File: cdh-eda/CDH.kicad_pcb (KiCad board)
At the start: 2 copper layers, 96 x 90 mm, 23 parts, among them J1 THD-20-R, J4 USB_OTG, P1 S04B-PASK-2(LF)(SN), P2 S04B-PASK-2(LF)(SN), U1 ATA6560-GAQW-VAO, U2 TPD2EUSB30, U3 MCP2510-E/SO, U4 74LVC1G07SE-7

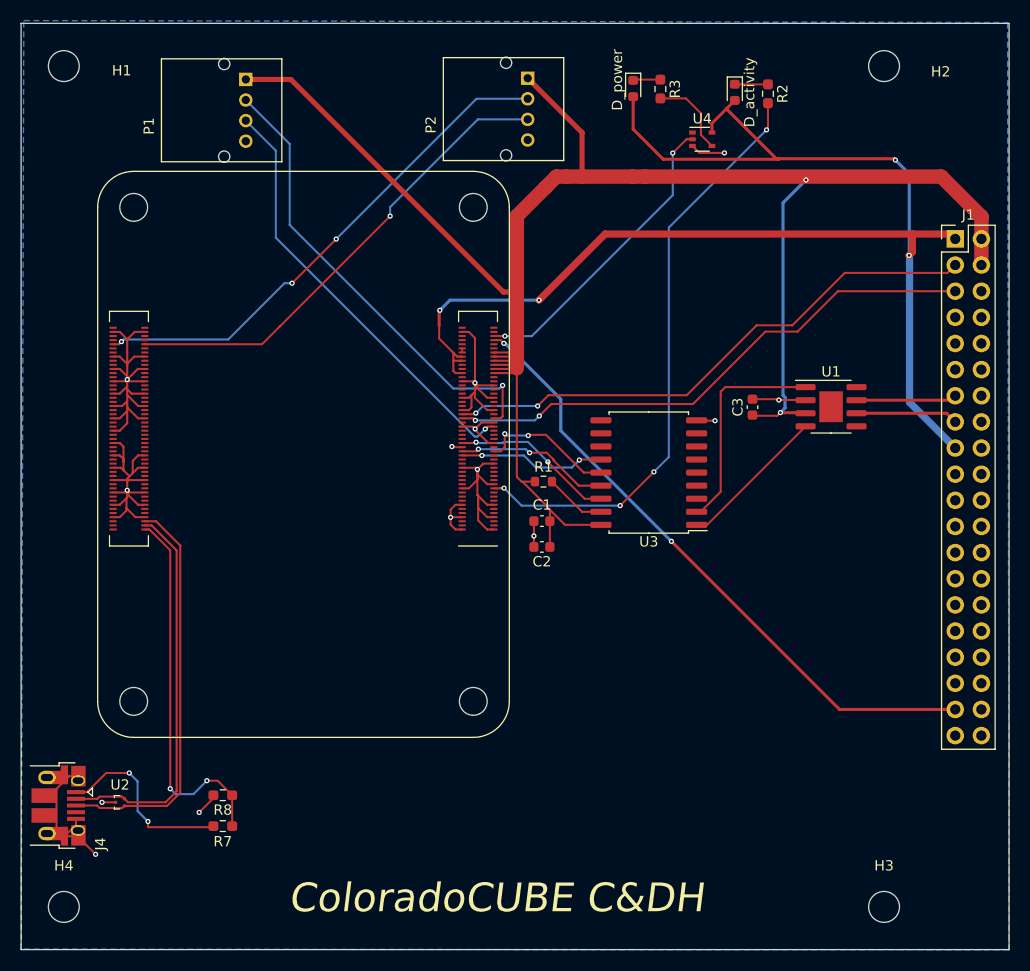
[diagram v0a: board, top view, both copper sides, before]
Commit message: V.2 updates
 1. Add jumper CAN resistors
 2. Add camera connector
 3. Add display connector
 5. Updated CAN transceiver protective circuitry
 6. Add MCP2515 interrupt GPIO pin 18
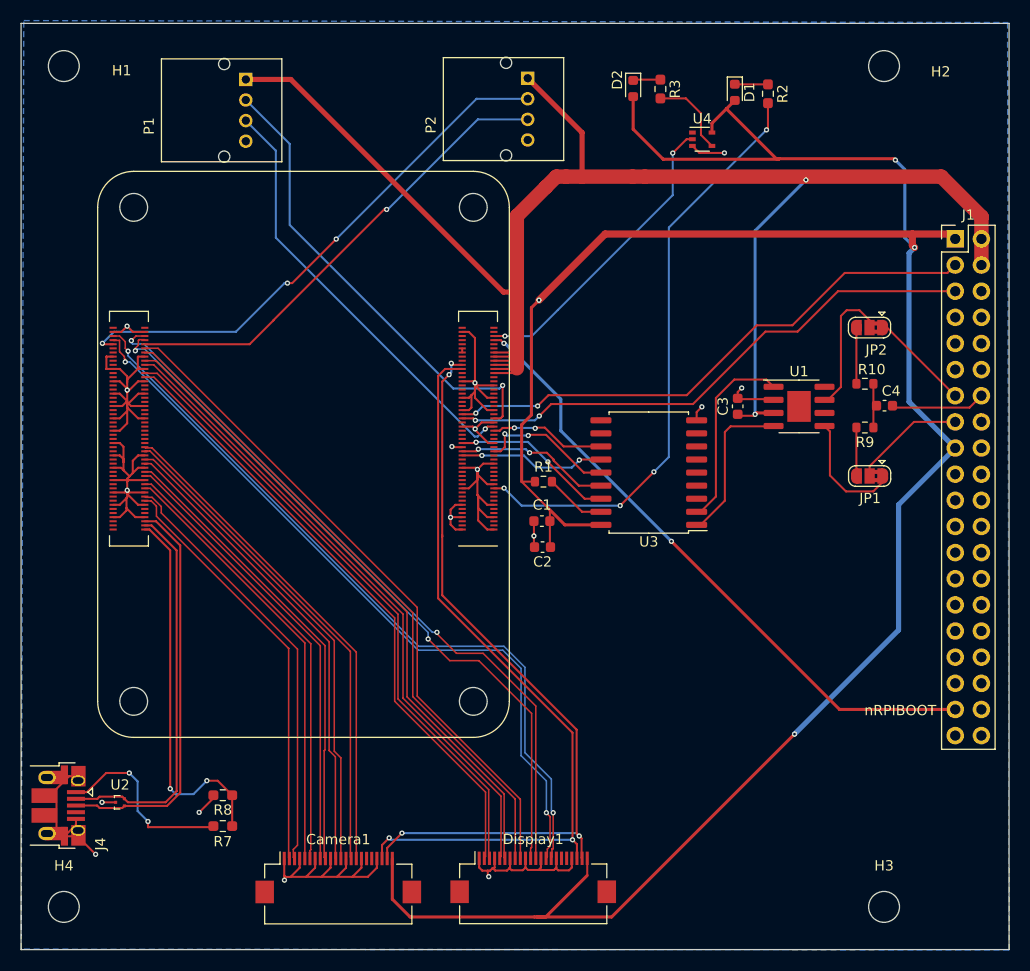
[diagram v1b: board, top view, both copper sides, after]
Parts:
- added C4: 4.7nF, Capacitor_SMD:C_0603_1608Metric, F.Cu at (190.4, 93.2)
- added Camera1: Conn_01x22_Female, Connector_FFC-FPC:Hirose_FH12-22S-0.5SH_1x22-1MP_P0.50mm_Horizontal, F.Cu at (137.3, 139.0)
- added Display1: Conn_01x22_Female, Connector_FFC-FPC:Hirose_FH12-22S-0.5SH_1x22-1MP_P0.50mm_Horizontal, F.Cu at (156.2, 139.0)
- added JP1: SolderJumper_3_Bridged12, Jumper:SolderJumper-3_P1.3mm_Bridged2Bar12_RoundedPad1.0x1.5mm, F.Cu at (188.9, 100.0)
- added JP2: SolderJumper_3_Bridged12, Jumper:SolderJumper-3_P1.3mm_Bridged2Bar12_RoundedPad1.0x1.5mm, F.Cu at (188.9, 85.6)
- added R10: 60, Resistor_SMD:R_0603_1608Metric, F.Cu at (188.5, 91.0)
- added R9: 60, Resistor_SMD:R_0603_1608Metric, F.Cu at (188.5, 95.3)
- Module1: value DF40GB-10DP-0.4V(51) -> ComputeModule4-CM4
- U2: value TPD2EUSB30 -> TPD2EUSB30ADRTR
- U3: value MCP2510-E/SO -> MCP2515T-I/SO
- moved U1 3.11 mm to (182.1, 93.2)
- moved C3 1.44 mm to (176.1, 93.2)
- moved C2 0.06 mm to (157.2, 106.9)
- renumbered D_activity to D1, D_power to D2
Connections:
- C1 pad 1: +5V -> +3.3V
- C2 pad 1: +5V -> +3.3V
- J1 pad 10: (no net) -> unconnected-(J1-Pad10)
- J1 pad 25: GND -> unconnected-(J1-Pad25)
- J1 pad 8: (no net) -> unconnected-(J1-Pad8)
- J1 pad 9: GND -> unconnected-(J1-Pad9)
- Module1 pad 10: Net-(Module1-Pad10) -> (no net)
- Module1 pad 100: Net-(Module1-Pad100) -> (no net)
- Module1 pad 102: Net-(Module1-Pad102) -> unconnected-(Module1-Pad102)
- Module1 pad 104: Net-(Module1-Pad104) -> unconnected-(Module1-Pad104)
- Module1 pad 106: Net-(Module1-Pad106) -> unconnected-(Module1-Pad106)
- Module1 pad 109: Net-(Module1-Pad109) -> unconnected-(Module1-Pad109)
- Module1 pad 11: Net-(Module1-Pad11) -> (no net)
- Module1 pad 110: Net-(Module1-Pad110) -> unconnected-(Module1-Pad110)
- Module1 pad 111: Net-(Module1-Pad111) -> unconnected-(Module1-Pad111)
- Module1 pad 112: Net-(Module1-Pad112) -> unconnected-(Module1-Pad112)
- Module1 pad 115: Net-(Module1-Pad115) -> /CM4 High Speed/CAM1_D0_N
- Module1 pad 116: Net-(Module1-Pad116) -> unconnected-(Module1-Pad116)
- Module1 pad 117: Net-(Module1-Pad117) -> /CM4 High Speed/CAM1_D0_P
- Module1 pad 118: Net-(Module1-Pad118) -> unconnected-(Module1-Pad118)
- Module1 pad 12: Net-(Module1-Pad12) -> (no net)
- Module1 pad 121: Net-(Module1-Pad121) -> /CM4 High Speed/CAM1_D1_N
- Module1 pad 122: Net-(Module1-Pad122) -> unconnected-(Module1-Pad122)
- Module1 pad 123: Net-(Module1-Pad123) -> /CM4 High Speed/CAM1_D1_P
- Module1 pad 124: Net-(Module1-Pad124) -> unconnected-(Module1-Pad124)
- Module1 pad 127: Net-(Module1-Pad127) -> /CM4 High Speed/CAM1_C_N
- Module1 pad 128: Net-(Module1-Pad128) -> unconnected-(Module1-Pad128)
- Module1 pad 129: Net-(Module1-Pad129) -> /CM4 High Speed/CAM1_C_P
- Module1 pad 130: Net-(Module1-Pad130) -> unconnected-(Module1-Pad130)
- Module1 pad 133: Net-(Module1-Pad133) -> /CM4 High Speed/CAM1_D2_N
- Module1 pad 134: Net-(Module1-Pad134) -> unconnected-(Module1-Pad134)
- Module1 pad 135: Net-(Module1-Pad135) -> /CM4 High Speed/CAM1_D2_P
- Module1 pad 136: Net-(Module1-Pad136) -> unconnected-(Module1-Pad136)
- Module1 pad 139: Net-(Module1-Pad139) -> /CM4 High Speed/CAM1_D3_N
- Module1 pad 140: Net-(Module1-Pad140) -> unconnected-(Module1-Pad140)
- Module1 pad 141: Net-(Module1-Pad141) -> /CM4 High Speed/CAM1_D3_P
- Module1 pad 142: Net-(Module1-Pad142) -> unconnected-(Module1-Pad142)
- Module1 pad 143: Net-(Module1-Pad143) -> unconnected-(Module1-Pad143)
- Module1 pad 145: Net-(Module1-Pad145) -> unconnected-(Module1-Pad145)
- Module1 pad 146: Net-(Module1-Pad146) -> unconnected-(Module1-Pad146)
- Module1 pad 147: Net-(Module1-Pad147) -> unconnected-(Module1-Pad147)
- Module1 pad 148: Net-(Module1-Pad148) -> unconnected-(Module1-Pad148)
- Module1 pad 149: Net-(Module1-Pad149) -> unconnected-(Module1-Pad149)
- Module1 pad 15: Net-(Module1-Pad15) -> (no net)
- Module1 pad 151: Net-(Module1-Pad151) -> unconnected-(Module1-Pad151)
- Module1 pad 152: Net-(Module1-Pad152) -> unconnected-(Module1-Pad152)
- Module1 pad 153: Net-(Module1-Pad153) -> unconnected-(Module1-Pad153)
- Module1 pad 154: Net-(Module1-Pad154) -> unconnected-(Module1-Pad154)
- Module1 pad 157: Net-(Module1-Pad157) -> unconnected-(Module1-Pad157)
- Module1 pad 158: Net-(Module1-Pad158) -> unconnected-(Module1-Pad158)
- Module1 pad 159: Net-(Module1-Pad159) -> unconnected-(Module1-Pad159)
- Module1 pad 16: Net-(Module1-Pad16) -> (no net)
- Module1 pad 160: Net-(Module1-Pad160) -> unconnected-(Module1-Pad160)
- Module1 pad 163: Net-(Module1-Pad163) -> unconnected-(Module1-Pad163)
- Module1 pad 164: Net-(Module1-Pad164) -> unconnected-(Module1-Pad164)
- Module1 pad 165: Net-(Module1-Pad165) -> unconnected-(Module1-Pad165)
- Module1 pad 166: Net-(Module1-Pad166) -> unconnected-(Module1-Pad166)
- Module1 pad 169: Net-(Module1-Pad169) -> unconnected-(Module1-Pad169)
- Module1 pad 17: Net-(Module1-Pad17) -> (no net)
- Module1 pad 170: Net-(Module1-Pad170) -> unconnected-(Module1-Pad170)
- Module1 pad 171: Net-(Module1-Pad171) -> unconnected-(Module1-Pad171)
- Module1 pad 172: Net-(Module1-Pad172) -> unconnected-(Module1-Pad172)
- Module1 pad 175: Net-(Module1-Pad175) -> /CM4 High Speed/DSI1_D0_N
- Module1 pad 176: Net-(Module1-Pad176) -> unconnected-(Module1-Pad176)
- Module1 pad 177: Net-(Module1-Pad177) -> /CM4 High Speed/DSI1_D0_P
- Module1 pad 178: Net-(Module1-Pad178) -> unconnected-(Module1-Pad178)
- Module1 pad 18: Net-(Module1-Pad18) -> (no net)
- Module1 pad 181: Net-(Module1-Pad181) -> /CM4 High Speed/DSI1_D1_N
- Module1 pad 182: Net-(Module1-Pad182) -> unconnected-(Module1-Pad182)
- Module1 pad 183: Net-(Module1-Pad183) -> /CM4 High Speed/DSI1_D1_P
- Module1 pad 184: Net-(Module1-Pad184) -> unconnected-(Module1-Pad184)
- Module1 pad 187: Net-(Module1-Pad187) -> /CM4 High Speed/DSI1_C_N
- Module1 pad 188: Net-(Module1-Pad188) -> unconnected-(Module1-Pad188)
- Module1 pad 189: Net-(Module1-Pad189) -> /CM4 High Speed/DSI1_C_P
- Module1 pad 19: Net-(Module1-Pad19) -> (no net)
- Module1 pad 190: Net-(Module1-Pad190) -> unconnected-(Module1-Pad190)
- Module1 pad 191: /CM4 GPIO/GPIO13 -> GND
- Module1 pad 192: /CM4 GPIO/GPIO12 -> GND
- Module1 pad 193: Net-(Module1-Pad193) -> /CM4 High Speed/DSI1_D2_N
- Module1 pad 194: Net-(Module1-Pad194) -> /CM4 High Speed/DSI1_D3_N
- Module1 pad 195: Net-(Module1-Pad195) -> /CM4 High Speed/DSI1_D2_P
- Module1 pad 196: Net-(Module1-Pad196) -> /CM4 High Speed/DSI1_D3_P
- Module1 pad 199: Net-(Module1-Pad199) -> unconnected-(Module1-Pad199)
- Module1 pad 20: /CM4 GPIO/EEPROM_nWP -> (no net)
- Module1 pad 200: Net-(Module1-Pad200) -> unconnected-(Module1-Pad200)
- Module1 pad 24: Net-(Module1-Pad24) -> (no net)
- Module1 pad 25: Net-(Module1-Pad25) -> (no net)
- Module1 pad 26: Net-(Module1-Pad26) -> (no net)
- Module1 pad 27: Net-(Module1-Pad27) -> (no net)
- Module1 pad 28: Net-(Module1-Pad28) -> (no net)
- Module1 pad 29: Net-(Module1-Pad29) -> (no net)
- Module1 pad 3: Net-(Module1-Pad3) -> (no net)
- Module1 pad 30: Net-(Module1-Pad30) -> (no net)
- Module1 pad 31: Net-(Module1-Pad31) -> (no net)
- Module1 pad 34: Net-(Module1-Pad34) -> (no net)
- Module1 pad 35: Net-(Module1-Pad35) -> (no net)
- Module1 pad 36: Net-(Module1-Pad36) -> (no net)
- Module1 pad 37: /CM4 GPIO/GPIO7 -> (no net)
- Module1 pad 4: Net-(Module1-Pad4) -> (no net)
- Module1 pad 41: Net-(Module1-Pad41) -> (no net)
- Module1 pad 45: Net-(Module1-Pad45) -> (no net)
- Module1 pad 46: Net-(Module1-Pad46) -> (no net)
- Module1 pad 47: Net-(Module1-Pad47) -> (no net)
- Module1 pad 48: Net-(Module1-Pad48) -> (no net)
- Module1 pad 49: Net-(Module1-Pad49) -> /CM4 GPIO/GPIO18
- Module1 pad 5: Net-(Module1-Pad5) -> (no net)
- Module1 pad 50: Net-(Module1-Pad50) -> (no net)
- Module1 pad 54: Net-(Module1-Pad54) -> (no net)
- Module1 pad 57: Net-(Module1-Pad57) -> (no net)
- Module1 pad 6: Net-(Module1-Pad6) -> (no net)
- Module1 pad 61: Net-(Module1-Pad61) -> (no net)
- Module1 pad 62: Net-(Module1-Pad62) -> (no net)
- Module1 pad 63: Net-(Module1-Pad63) -> (no net)
- Module1 pad 64: Net-(Module1-Pad64) -> (no net)
- Module1 pad 67: Net-(Module1-Pad67) -> (no net)
- Module1 pad 68: Net-(Module1-Pad68) -> (no net)
- Module1 pad 69: Net-(Module1-Pad69) -> (no net)
- Module1 pad 70: Net-(Module1-Pad70) -> (no net)
- Module1 pad 72: Net-(Module1-Pad72) -> (no net)
- Module1 pad 73: Net-(Module1-Pad73) -> (no net)
- Module1 pad 75: Net-(Module1-Pad75) -> (no net)
- Module1 pad 76: Net-(Module1-Pad76) -> (no net)
- Module1 pad 78: +3.3V -> (no net)
- Module1 pad 80: Net-(Module1-Pad80) -> /CM4 High Speed/SCL0
- Module1 pad 82: Net-(Module1-Pad82) -> /CM4 High Speed/SDA0
- Module1 pad 84: +3.3V -> (no net)
- Module1 pad 86: +3.3V -> (no net)
- Module1 pad 88: +1.8V -> (no net)
- Module1 pad 89: Net-(Module1-Pad89) -> (no net)
- Module1 pad 9: Net-(Module1-Pad9) -> (no net)
- Module1 pad 90: +1.8V -> (no net)
- Module1 pad 91: Net-(Module1-Pad91) -> (no net)
- Module1 pad 92: Net-(Module1-Pad92) -> (no net)
- Module1 pad 94: Net-(Module1-Pad94) -> (no net)
- Module1 pad 96: Net-(Module1-Pad96) -> (no net)
- Module1 pad 97: Net-(Module1-Pad97) -> (no net)
- Module1 pad 99: Net-(Module1-Pad99) -> (no net)
- R1 pad 1: +5V -> +3.3V
- U1 pad 5: unconnected-(U1-Pad5) -> Net-(U1-Pad5)
- U1 pad 6: Net-(J1-Pad15) -> unconnected-(U1-Pad6)
- U1 pad 7: Net-(J1-Pad13) -> Net-(U1-Pad7)
- U3 pad 12: unconnected-(U3-Pad12) -> /CM4 GPIO/GPIO18
- U3 pad 18: +5V -> +3.3V
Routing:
- net GND: track 146.9 -> 292.3 mm, vias 14 -> 21
- net +3.3V: track 136.7 -> 243.6 mm
- net /CM4 High Speed/SDA0: track 0.00 -> 75.8 mm, vias 0 -> 4
- net /CM4 High Speed/SCL0: track 0.00 -> 75.3 mm, vias 0 -> 2
- net /CM4 High Speed/DSI1_D3_P: track 0.00 -> 73.8 mm, vias 0 -> 2
- net /CM4 High Speed/DSI1_D3_N: track 0.00 -> 73.5 mm, vias 0 -> 2
- net /CM4 High Speed/DSI1_D2_P: track 0.00 -> 70.5 mm, vias 0 -> 2
- net /CM4 High Speed/DSI1_D2_N: track 0.00 -> 69.5 mm, vias 0 -> 2
- net /CM4 High Speed/DSI1_C_P: track 0.00 -> 65.4 mm
- net /CM4 High Speed/DSI1_C_N: track 0.00 -> 64.5 mm
- net /CM4 High Speed/DSI1_D1_P: track 0.00 -> 63.5 mm
- net /CM4 High Speed/DSI1_D1_N: track 0.00 -> 62.8 mm
- net /CM4 High Speed/DSI1_D0_P: track 0.00 -> 61.7 mm
- net /CM4 High Speed/DSI1_D0_N: track 0.00 -> 61.0 mm
- net /CM4 GPIO/GPIO12: track 50.2 -> 0.00 mm, vias 3 -> 0
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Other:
- board text added: "nRPIBOOT"
- board text removed: "ColoradoCUBE C&DH"
- board text removed: "Wireless Keepout"
